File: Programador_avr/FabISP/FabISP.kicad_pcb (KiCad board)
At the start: 2 copper layers, 41 x 19 mm, 14 parts, among them IC1 ATTINY44-SSU, M1 Reson., M2 PINHD-1x02-SMD-HEADER, M3 MICRO-USB_1_64, M4 PINHD-1x02-SMD-HEADER

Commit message: cambios y correcciones listas para revisión de compañero y docente
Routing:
- net (no net): track 5.46 -> 0.00 mm
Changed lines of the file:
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@@
     (thickness 1.6)
     (drawings 9)
-    (tracks 153)
+    (tracks 149)
     (zones 0)
     (modules 14)
@@
   (gr_line (start 166.5 87.5) (end 166.5 106.5) (layer Edge.Cuts) (width 0.05))
   (gr_line (start 126.5 87.5) (end 166.5 87.5) (layer Edge.Cuts) (width 0.05))
-  (segment (start 128.5 92.75) (end 131.25 92.75) (width 0.25) (layer F.Cu) (net 0))
-  (segment (start 131.25 92.75) (end 131.110101 92.889899) (width 0.25) (layer F.Cu) (net 0))
-  (segment (start 130.75 101) (end 131.110101 100.639899) (width 0.25) (layer F.Cu) (net 0))
-  (segment (start 128.75 101) (end 130.75 101) (width 0.25) (layer F.Cu) (net 0))
   (segment (start 133 94.75) (end 132.29794 95.45206) (width 0.25) (layer F.Cu) (net 1))
   (segment (start 140.45001 88.29999) (end 139.5 89.25) (width 0.25) (layer F.Cu) (net 1))
@@
     (connect_pads (clearance 0.508))
     (min_thickness 0.254)
+    (fill yes (arc_segments 32) (thermal_gap 0.508) (thermal_bridge_width 0.508))
+    (polygon
+      (pts
+        (xy 125.5 87.5) (xy 125.5 106.5) (xy 166.5 106.5) (xy 166.5 87.5)
+      )
+    )
+  )
+  (zone (net 0) (net_name "") (layer F.Cu) (hatch edge 0.508)
+    (connect_pads (clearance 0.508))
+    (min_thickness 0.254)

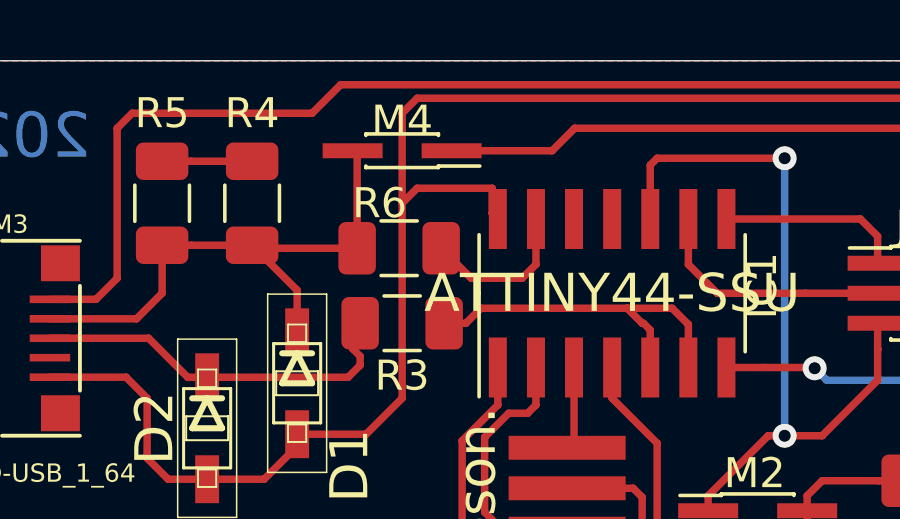
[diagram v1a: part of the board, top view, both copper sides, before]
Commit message: mejora de vistas
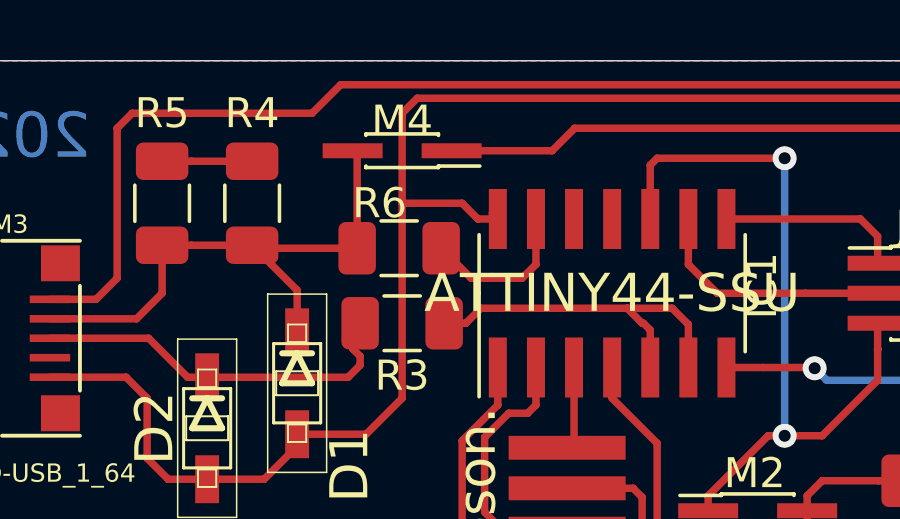
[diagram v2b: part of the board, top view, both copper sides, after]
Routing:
- net GND: track 87.7 -> 87.1 mm
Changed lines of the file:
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@@
   (segment (start 139 100.34931) (end 137.90005 101.44926) (width 0.25) (layer F.Cu) (net 2) (status 10))
   (segment (start 139 99.94926) (end 139 100.34931) (width 0.25) (layer F.Cu) (net 2) (status 30))
-  (segment (start 145.5 91.75) (end 145.5 92.585) (width 0.25) (layer F.Cu) (net 2) (status 20))
   (segment (start 145.5 92.585) (end 145.69 92.775) (width 0.25) (layer F.Cu) (net 2) (status 30))
-  (segment (start 143 91.75) (end 145.5 91.75) (width 0.25) (layer F.Cu) (net 2))
-  (segment (start 142.5 92.25) (end 143 91.75) (width 0.25) (layer F.Cu) (net 2))
   (segment (start 142.5 98.75) (end 142.5 92.25) (width 0.25) (layer F.Cu) (net 2))
   (segment (start 141.30074 99.94926) (end 142.5 98.75) (width 0.25) (layer F.Cu) (net 2))
@@
   (segment (start 158.375 104) (end 157.625 104.75) (width 0.25) (layer F.Cu) (net 2))
   (segment (start 157.625 104.75) (end 150.75 104.75) (width 0.25) (layer F.Cu) (net 2))
+  (segment (start 144.5 92.25) (end 142.5 92.25) (width 0.25) (layer F.Cu) (net 2))
+  (segment (start 145.025 92.775) (end 144.5 92.25) (width 0.25) (layer F.Cu) (net 2))
+  (segment (start 145.69 92.775) (end 145.025 92.775) (width 0.25) (layer F.Cu) (net 2))
   (segment (start 134.5 95.25) (end 134.5 93.65) (width 0.25) (layer F.Cu) (net 3) (status 20))
   (segment (start 133.6477 96.1023) (end 134.5 95.25) (width 0.25) (layer F.Cu) (net 3))

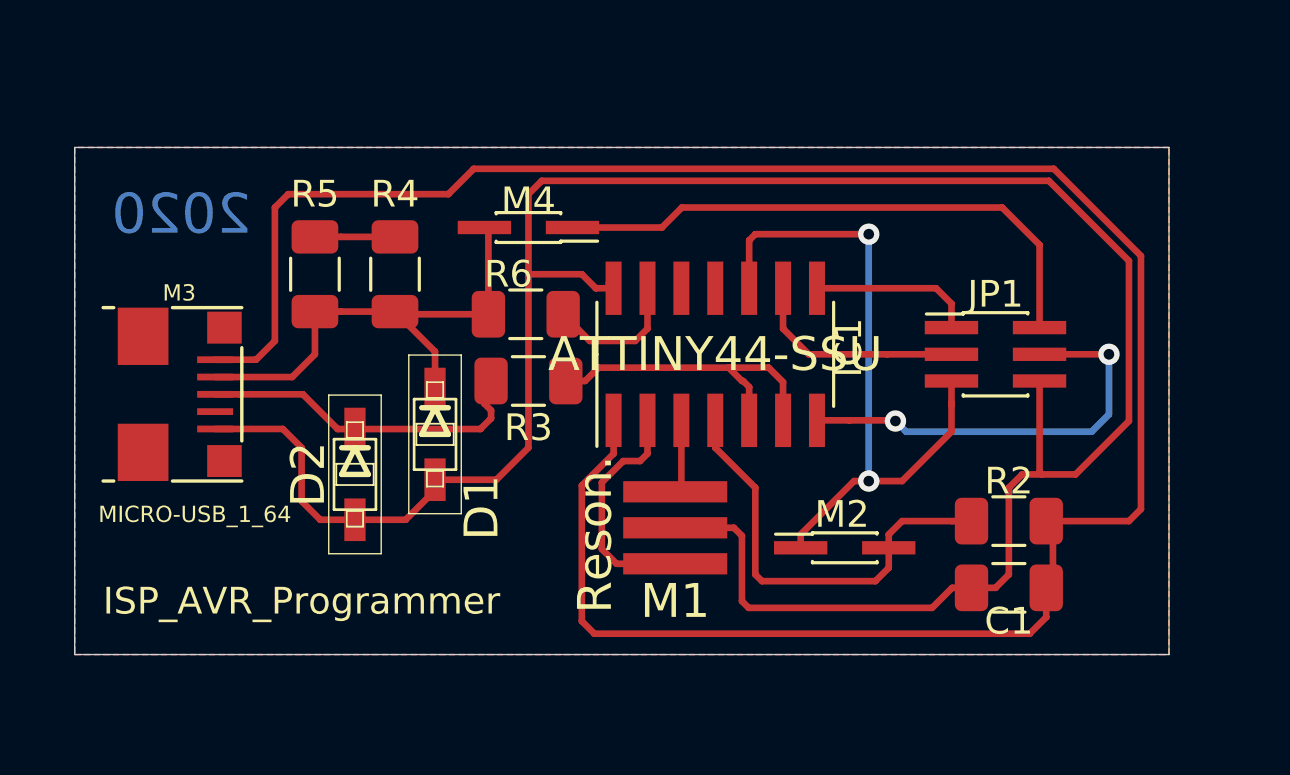
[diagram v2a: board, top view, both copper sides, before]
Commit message: Se corrigió todas las vías al tamaño sugerido, se mejoró la ubicación de componentes sugeridos, se realizaron cambios en las vías
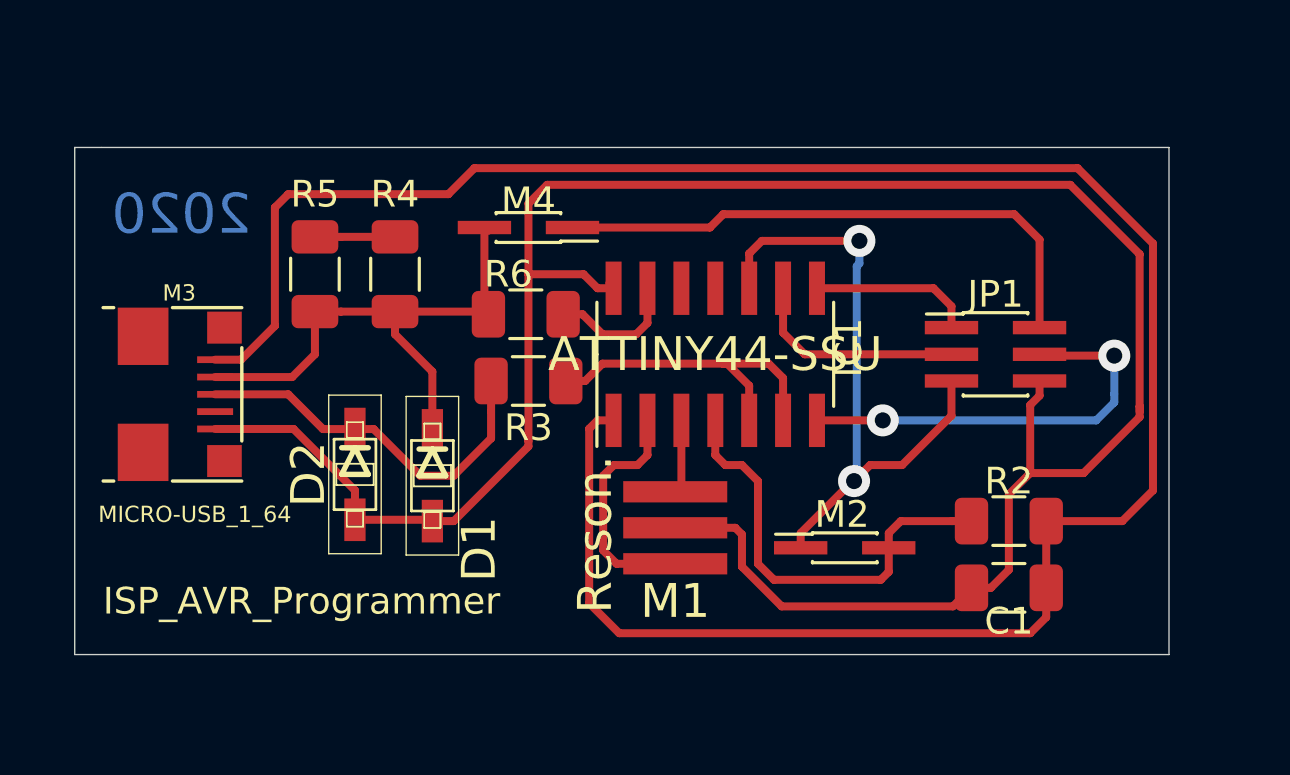
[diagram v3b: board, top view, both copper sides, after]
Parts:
- moved D1 1.55 mm to (138.9, 99.8)
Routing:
- net /D-: track 19.1 -> 20.9 mm
- net /D+: track 12.5 -> 14.3 mm
- net /RST: track 25.3 -> 24.0 mm
- net GND: track 87.1 -> 85.8 mm
- net /SCK: track 7.33 -> 8.31 mm
- net Net-(IC1-Pad5): track 12.3 -> 12.8 mm
- removed copper zone on B.Cu, net (none)
- removed copper zone on F.Cu, net (none)

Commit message: Se hicieron los cambios sugeridos de ubicación de componentes asi como aproximaciín de circuito integrado a usb
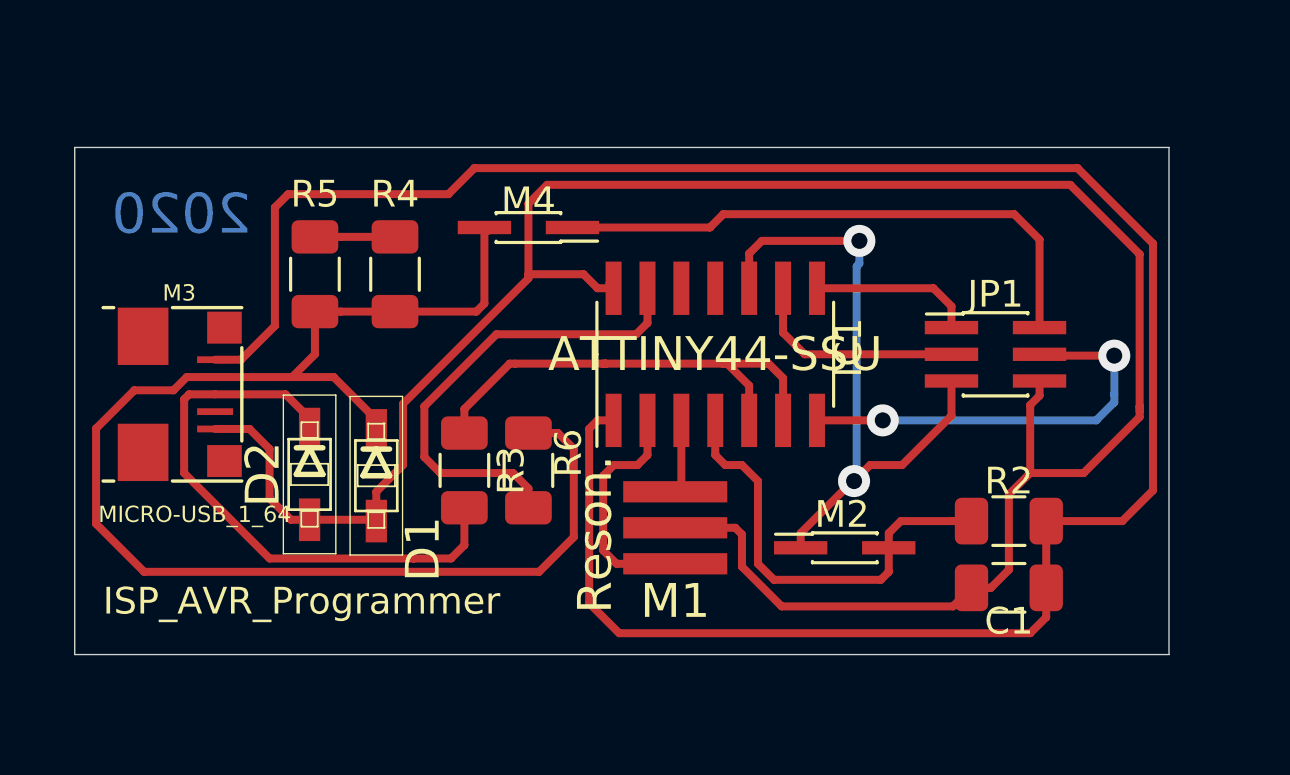
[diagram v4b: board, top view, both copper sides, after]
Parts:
- moved R6 5.85 mm to (142.5, 99.6), turned to 270 degrees
- moved R3 4.12 mm to (140.1, 99.6), turned to 90 degrees
- moved D1 2.10 mm to (136.8, 99.8)
- moved D2 1.70 mm to (134.3, 99.8)
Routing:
- net /D-: track 20.9 -> 52.8 mm
- net Net-(IC1-Pad13): track 4.95 -> 18.0 mm
- net /D+: track 14.3 -> 21.7 mm
- net Net-(IC1-Pad5): track 12.8 -> 18.1 mm
- net GND: track 85.8 -> 84.6 mm

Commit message: se agrego componentes en 3D se corrigió nodo tierra y esquemático, se agregó agujero de sujeción
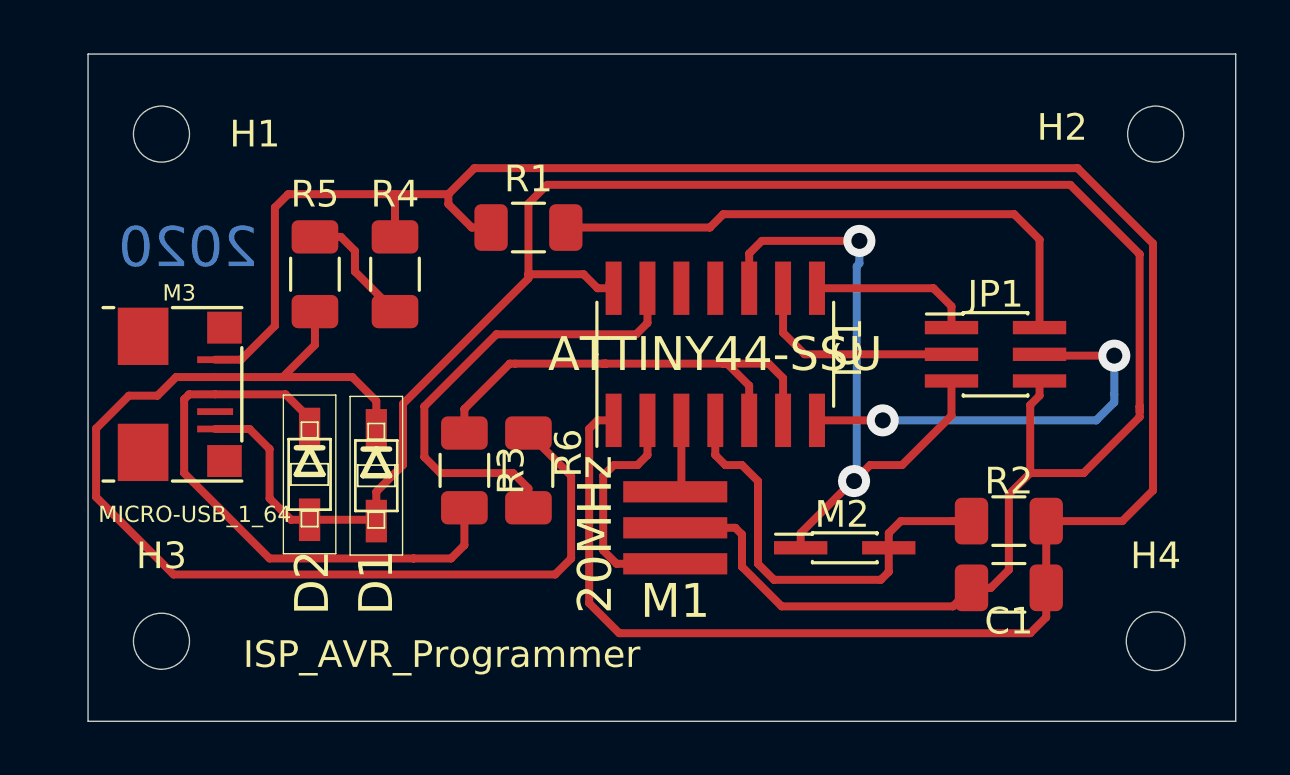
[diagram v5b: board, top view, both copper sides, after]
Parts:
- removed M4: PINHD-1x02-SMD-HEADER, Connector_PinHeader_1.00mm:PinHeader_2x01_P1.00mm_Vertical_SMD
- added H1: MountingHole, MountingHole:MountingHole_2.1mm, F.Cu at (128.8, 87.0)
- added H2: MountingHole, MountingHole:MountingHole_2.1mm, F.Cu at (166.0, 87.0)
- added H3: MountingHole, MountingHole:MountingHole_2.1mm, F.Cu at (128.8, 106.0)
- added H4: MountingHole, MountingHole:MountingHole_2.2mm_M2, F.Cu at (166.0, 106.0)
- added R1: 0, Resistor_SMD:R_1206_3216Metric, F.Cu at (142.5, 90.5)
- D1, D2: value (none) -> 3.3V
- M1: value Reson. -> 20MHz
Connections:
- net /D+ renamed Net-(D2-PadCATHODE)
- D1 pad CATHODE: /D- -> Net-(D1-PadCATHODE)
- M3 pad D-: /D- -> Net-(D1-PadCATHODE)
- R4 pad 2: /D- -> Net-(D1-PadCATHODE)
- R5 pad 1: /D- -> Net-(R4-Pad1)
- R5 pad 2: Net-(R4-Pad1) -> VCC
- R6 pad 1: /D- -> Net-(D1-PadCATHODE)
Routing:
- net /D-: track 52.8 -> 0.00 mm
- net Net-(D1-PadCATHODE): track 0.00 -> 42.9 mm
- net VCC: track 84.6 -> 88.6 mm
- net Net-(R4-Pad1): track 3.00 -> 4.61 mm
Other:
- board size 41 x 19 mm -> 43 x 25 mm

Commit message: acomodado de componentes
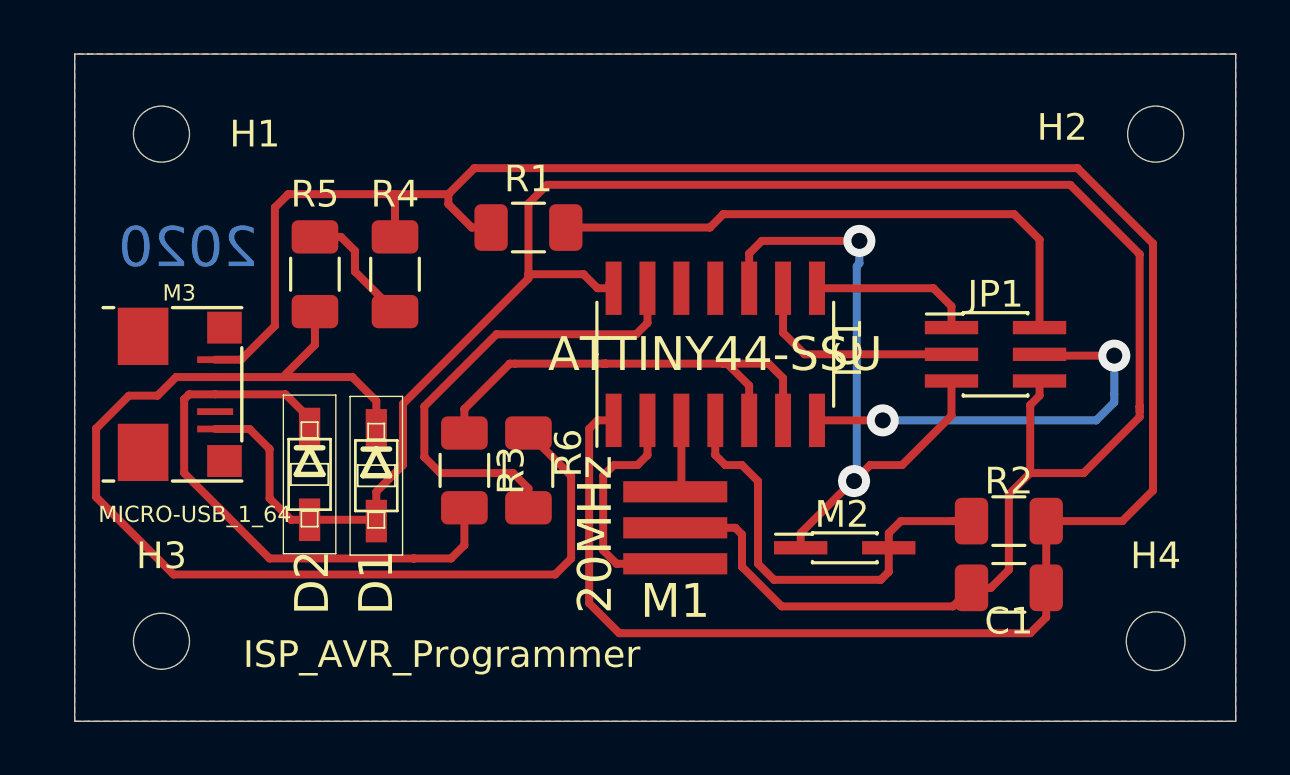
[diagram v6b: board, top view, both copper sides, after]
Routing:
- added copper zone on B.Cu, net (none)
- added copper zone on F.Cu, net GND
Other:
- board size 43 x 25 mm -> 43.5 x 25 mm
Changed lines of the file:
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@@
   (general
     (thickness 1.6)
-    (drawings 6)
+    (drawings 8)
     (tracks 176)
     (zones 0)
@@
     (pad "" np_thru_hole circle (at 0 0) (size 2.1 2.1) (drill 2.1) (layers *.Cu *.Mask))
   )
+  (gr_line (start 125.5 84) (end 126 84) (layer Edge.Cuts) (width 0.05))
+  (gr_line (start 125.5 109) (end 125.5 84) (layer Edge.Cuts) (width 0.05))
+  (gr_line (start 126 109) (end 125.5 109) (layer Edge.Cuts) (width 0.05))
   (gr_line (start 126 109) (end 169 109) (layer Edge.Cuts) (width 0.05))
-  (gr_line (start 126 84) (end 126 109) (layer Edge.Cuts) (width 0.05))
   (gr_line (start 169 84) (end 126 84) (layer Edge.Cuts) (width 0.05))
   (gr_line (start 169 84) (end 169 109) (layer Edge.Cuts) (width 0.05))
@@
   (segment (start 129.6 96.935211) (end 129.6 99.7) (width 0.3) (layer F.Cu) (net 17))
   (segment (start 130.759581 96.75) (end 129.785211 96.75) (width 0.3) (layer F.Cu) (net 17) (status 10))
+  (zone (net 2) (net_name GND) (layer F.Cu) (hatch edge 0.508)
+    (connect_pads (clearance 0.508))
+    (min_thickness 0.254)
+    (fill yes (arc_segments 32) (thermal_gap 0.508) (thermal_bridge_width 0.508))
+    (polygon
+      (pts
+        (xy 125.5 84) (xy 125.5 109) (xy 169 109) (xy 169 84)
+      )
+    )
+  )
+  (zone (net 0) (net_name "") (layer B.Cu) (hatch edge 0.508)
+    (connect_pads (clearance 0.508))
+    (min_thickness 0.254)
+    (fill yes (arc_segments 32) (thermal_gap 0.508) (thermal_bridge_width 0.508))
+    (polygon
+      (pts
+        (xy 125.5 84) (xy 125.5 109) (xy 169 109) (xy 169 84)
+      )
+    )
+  )
 )
